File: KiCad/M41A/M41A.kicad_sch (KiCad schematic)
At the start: 22 parts, among them SW1 SW_PWR_ON_OFF

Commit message: Updated scheme
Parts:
- C3: footprint Capacitor_THT:C_Disc_D3.0mm_W2.0mm_P2.50mm -> Capacitor_THT:CP_Radial_D5.0mm_P2.50mm
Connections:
- net at DRV-74HC595.1 (VCC): now also A1.27 (+5V), C1.1, C2.1, D1.1 (K), D2.2 (A), RE1.5 (VCC)
- net at DRV-74HC595.3 (SDD): now also A1.16 (D13)
- net at DRV-74HC595.4 (SCLK): now also A1.14 (D11)
- net at DRV-74HC595.5 (LOAD): now also A1.15 (D12)
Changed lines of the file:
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@@
 			)
 		)
-		(property "Footprint" "Capacitor_THT:C_Disc_D3.0mm_W2.0mm_P2.50mm"
+		(property "Footprint" "Capacitor_THT:CP_Radial_D5.0mm_P2.50mm"
 			(at 74.93 122.8852 0)
 			(effects

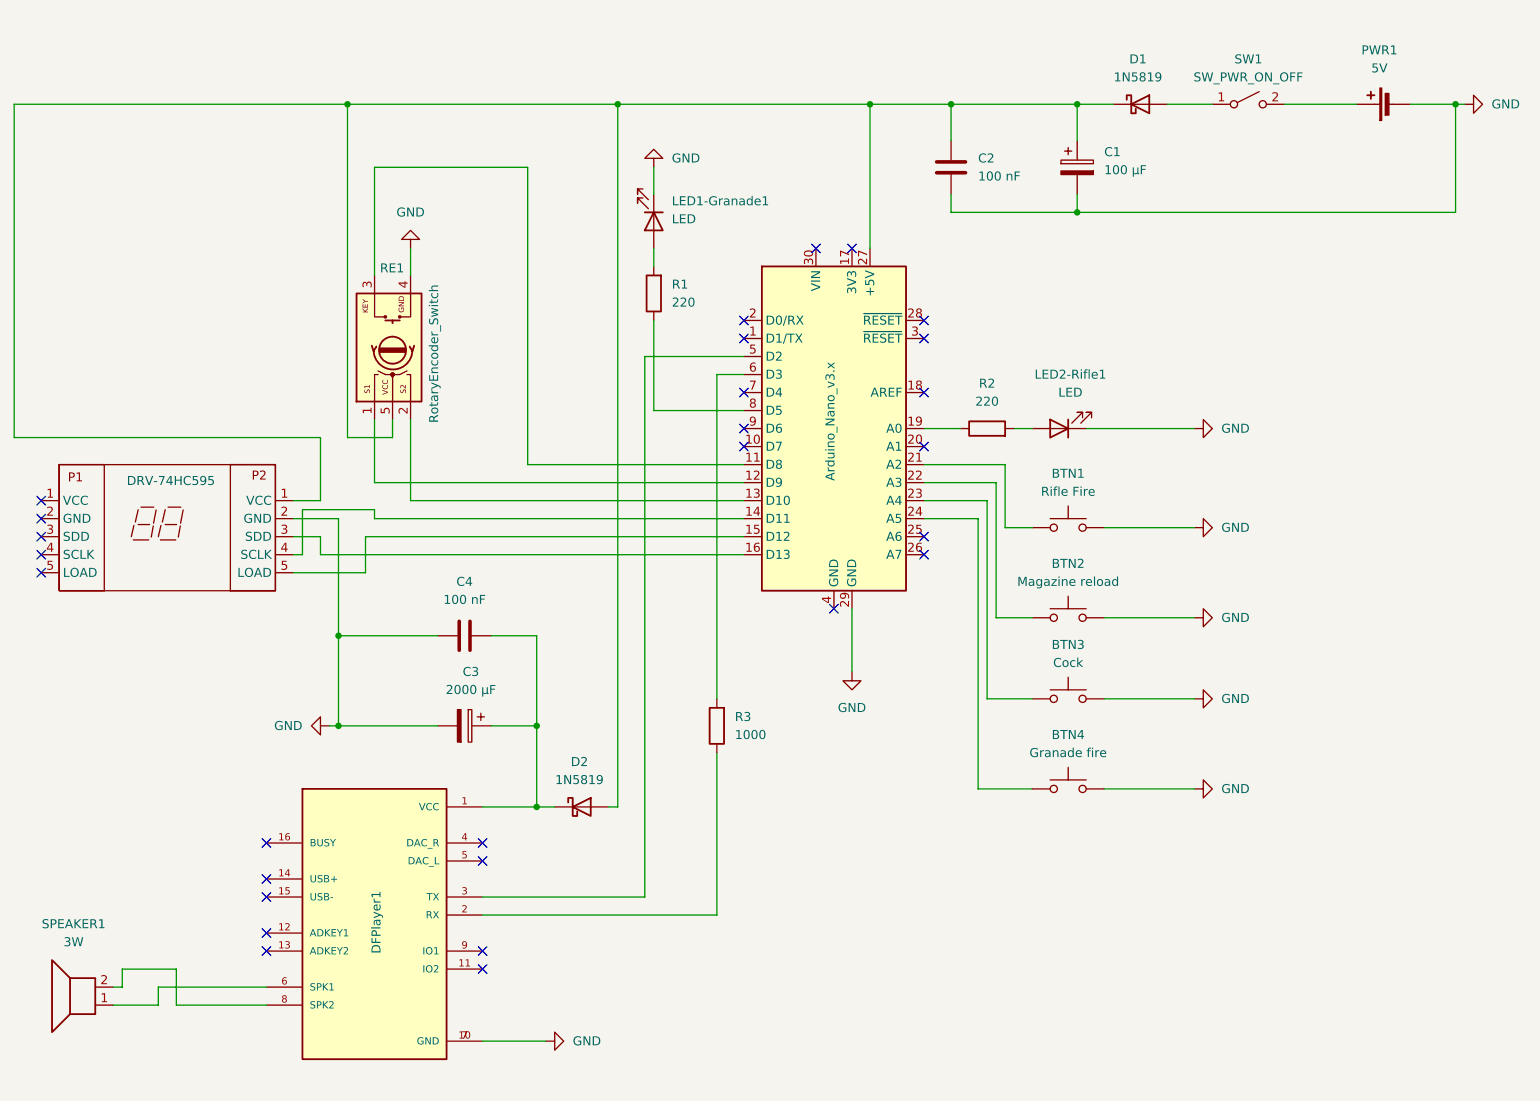
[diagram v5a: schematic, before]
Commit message: Corrected schema wiring between arduino and df player.
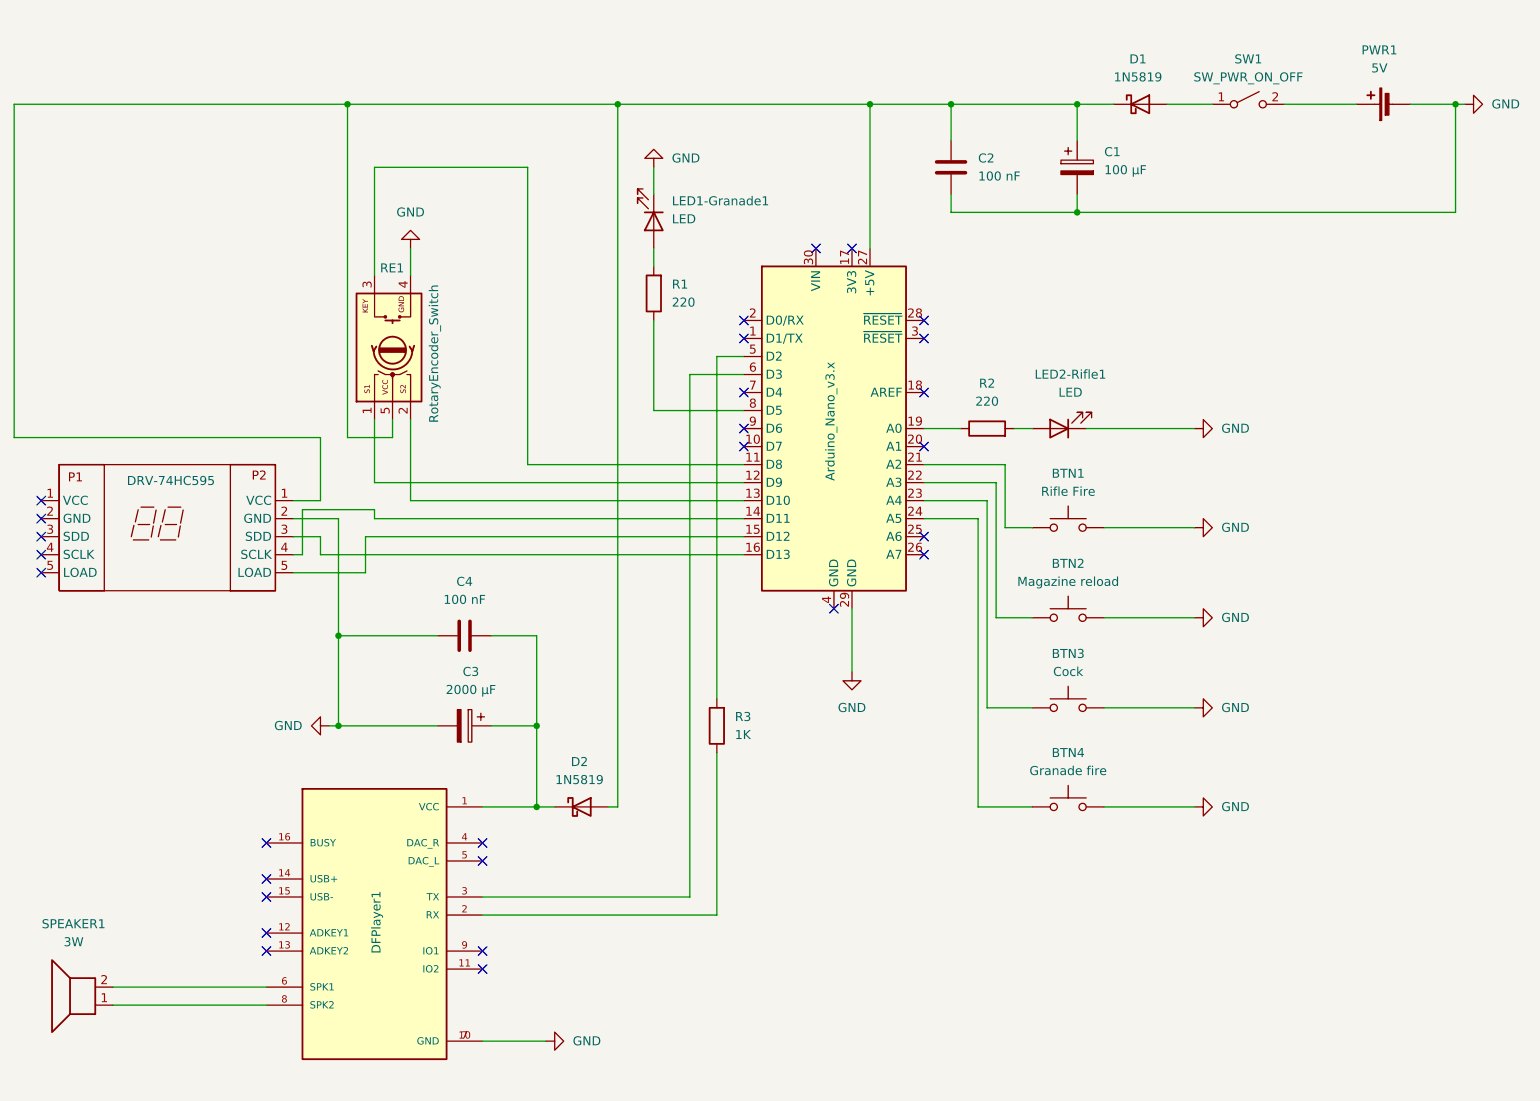
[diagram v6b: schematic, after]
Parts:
- R3: value 1000 -> 1K
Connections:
- net at SPEAKER1.1: now also DFPlayer1.8 (SPK2); no longer DFPlayer1.6 (SPK1)
- net at SPEAKER1.2: now also DFPlayer1.6 (SPK1); no longer DFPlayer1.8 (SPK2)
- net at DRV-74HC595.1 (VCC): now also A1.27 (+5V), C1.1, C2.1, D1.1 (K), D2.2 (A), RE1.5 (VCC)
- net at DRV-74HC595.3 (SDD): now also A1.16 (D13)
- net at DRV-74HC595.4 (SCLK): now also A1.14 (D11)
- net at DRV-74HC595.5 (LOAD): now also A1.15 (D12)
- net at R3.2: now also A1.5 (D2); no longer A1.6 (D3)
- net at DFPlayer1.3 (TX): now also A1.6 (D3); no longer A1.5 (D2)
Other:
- moved on the sheet: BTN3, BTN4
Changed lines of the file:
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@@
 		(date "2024-05-20")
 		(rev "1.1")
-		(comment 1 "https://github.com/ByPS128/Arduino-Aliens-M41A-Riffle")
+		(comment 1 "https://github.com/ByPS128/Arduino-Aliens-M41A-Rifle")
 		(comment 2 "Developer: Petr Škaloud aka ByPS")
 	)
@@
 	(wire
 		(pts
-			(xy 151.13 130.81) (xy 151.13 92.71)
+			(xy 151.13 133.35) (xy 151.13 92.71)
 		)
 		(stroke
@@
 	(wire
 		(pts
-			(xy 152.4 118.11) (xy 158.75 118.11)
+			(xy 152.4 119.38) (xy 158.75 119.38)
 		)
 		(stroke
@@
 	(wire
 		(pts
-			(xy 114.3 72.39) (xy 114.3 118.11)
+			(xy 114.3 69.85) (xy 114.3 118.11)
 		)
 		(stroke
@@
 	(wire
 		(pts
-			(xy 104.14 146.05) (xy 81.28 146.05)
+			(xy 110.49 146.05) (xy 81.28 146.05)
 		)
 		(stroke
@@
 	(wire
 		(pts
-			(xy 66.04 91.44) (xy 66.04 92.71)
+			(xy 110.49 72.39) (xy 110.49 146.05)
 		)
 		(stroke
@@
 	(wire
 		(pts
-			(xy 82.55 109.22) (xy 88.9 109.22)
-		)
-		(stroke
-			(width 0)
-			(type default)
-		)
-	)
-	(wire
-		(pts
-			(xy 143.51 87.63) (xy 153.67 87.63)
+			(xy 66.04 91.44) (xy 66.04 92.71)
 		)
 		(stroke
@@
 	(wire
 		(pts
-			(xy 165.1 34.29) (xy 170.18 34.29)
+			(xy 82.55 109.22) (xy 88.9 109.22)
 		)
 		(stroke
@@
 	(wire
 		(pts
-			(xy 88.9 109.22) (xy 88.9 121.92)
+			(xy 143.51 87.63) (xy 153.67 87.63)
 		)
 		(stroke
@@
 	(wire
 		(pts
-			(xy 35.56 161.29) (xy 29.21 161.29)
+			(xy 165.1 34.29) (xy 170.18 34.29)
 		)
 		(stroke
@@
 	(wire
 		(pts
-			(xy 35.56 158.75) (xy 50.8 158.75)
+			(xy 88.9 109.22) (xy 88.9 121.92)
 		)
 		(stroke
@@
 	(wire
 		(pts
-			(xy 50.8 161.29) (xy 38.1 161.29)
+			(xy 29.21 161.29) (xy 50.8 161.29)
 		)
 		(stroke
@@
 	(wire
 		(pts
-			(xy 35.56 158.75) (xy 35.56 161.29)
-		)
-		(stroke
-			(width 0)
-			(type default)
-		)
-	)
-	(wire
-		(pts
 			(xy 74.93 109.22) (xy 60.96 109.22)
 		)
@@
 	(wire
 		(pts
-			(xy 158.75 130.81) (xy 151.13 130.81)
+			(xy 158.75 133.35) (xy 151.13 133.35)
 		)
 		(stroke
@@
 	(wire
 		(pts
-			(xy 104.14 69.85) (xy 104.14 146.05)
-		)
-		(stroke
-			(width 0)
-			(type default)
-		)
-	)
-	(wire
-		(pts
 			(xy 15.24 34.29) (xy 62.23 34.29)
 		)
@@
 	(wire
 		(pts
-			(xy 114.3 72.39) (xy 118.11 72.39)
-		)
-		(stroke
-			(width 0)
-			(type default)
-		)
-	)
-	(wire
-		(pts
 			(xy 218.44 34.29) (xy 218.44 49.53)
 		)
@@
 	(wire
 		(pts
-			(xy 168.91 130.81) (xy 181.61 130.81)
+			(xy 168.91 133.35) (xy 181.61 133.35)
 		)
 		(stroke
@@
 	(wire
 		(pts
-			(xy 168.91 118.11) (xy 181.61 118.11)
+			(xy 168.91 119.38) (xy 181.61 119.38)
 		)
 		(stroke
@@
 	(wire
 		(pts
-			(xy 166.37 80.01) (xy 181.61 80.01)
+			(xy 110.49 72.39) (xy 118.11 72.39)
 		)
 		(stroke
@@
 	(wire
 		(pts
-			(xy 54.61 100.33) (xy 64.77 100.33)
+			(xy 166.37 80.01) (xy 181.61 80.01)
 		)
 		(stroke
@@
 	(wire
 		(pts
-			(xy 147.32 34.29) (xy 147.32 39.37)
+			(xy 54.61 100.33) (xy 64.77 100.33)
 		)
 		(stroke
@@
 	(wire
 		(pts
-			(xy 88.9 133.35) (xy 91.44 133.35)
+			(xy 147.32 34.29) (xy 147.32 39.37)
 		)
 		(stroke
@@
 	(wire
 		(pts
-			(xy 135.89 34.29) (xy 147.32 34.29)
+			(xy 88.9 133.35) (xy 91.44 133.35)
 		)
 		(stroke
@@
 	(wire
 		(pts
-			(xy 62.23 81.28) (xy 62.23 34.29)
+			(xy 135.89 34.29) (xy 147.32 34.29)
 		)
 		(stroke
@@
 	(wire
 		(pts
-			(xy 147.32 34.29) (xy 165.1 34.29)
+			(xy 62.23 81.28) (xy 62.23 34.29)
 		)
 		(stroke
@@
 	(wire
 		(pts
-			(xy 118.11 69.85) (xy 104.14 69.85)
+			(xy 147.32 34.29) (xy 165.1 34.29)
 		)
 		(stroke
@@
 	(wire
 		(pts
-			(xy 38.1 161.29) (xy 38.1 156.21)
-		)
-		(stroke
-			(width 0)
-			(type default)
-		)
-	)
-	(wire
-		(pts
 			(xy 66.04 87.63) (xy 118.11 87.63)
 		)
@@
 	(wire
 		(pts
-			(xy 30.48 156.21) (xy 30.48 158.75)
-		)
-		(stroke
-			(width 0)
-			(type default)
-		)
-	)
-	(wire
-		(pts
 			(xy 135.89 34.29) (xy 135.89 54.61)
 		)
@@
 	(wire
 		(pts
-			(xy 30.48 158.75) (xy 29.21 158.75)
+			(xy 29.21 158.75) (xy 50.8 158.75)
 		)
 		(stroke
@@
 	(wire
 		(pts
-			(xy 152.4 90.17) (xy 152.4 118.11)
+			(xy 152.4 90.17) (xy 152.4 119.38)
 		)
 		(stroke
@@
 	(wire
 		(pts
-			(xy 38.1 156.21) (xy 30.48 156.21)
+			(xy 153.67 106.68) (xy 158.75 106.68)
 		)
 		(stroke
@@
 	(wire
 		(pts
-			(xy 153.67 106.68) (xy 158.75 106.68)
+			(xy 55.88 91.44) (xy 66.04 91.44)
 		)
 		(stroke
@@
 	(wire
 		(pts
-			(xy 55.88 91.44) (xy 66.04 91.44)
+			(xy 88.9 121.92) (xy 88.9 133.35)
 		)
 		(stroke
@@
 	(wire
 		(pts
-			(xy 88.9 121.92) (xy 88.9 133.35)
+			(xy 212.09 34.29) (xy 218.44 34.29)
 		)
 		(stroke
@@
 	(wire
 		(pts
-			(xy 212.09 34.29) (xy 218.44 34.29)
+			(xy 153.67 87.63) (xy 153.67 106.68)
 		)
 		(stroke
@@
 	(wire
 		(pts
-			(xy 153.67 87.63) (xy 153.67 106.68)
+			(xy 114.3 69.85) (xy 118.11 69.85)
 		)
 		(stroke
@@
 	(symbol
 		(lib_id "Switch:SW_Push")
-		(at 163.83 118.11 0)
+		(at 163.83 119.38 0)
 		(unit 1)
 		(exclude_from_sim no)
@@
 		(fields_autoplaced yes)
 		(property "Reference" "BTN3"
-			(at 163.83 110.49 0)
+			(at 163.83 111.76 0)
 			(effects
 				(font
@@
 		)
 		(property "Value" "Cock"
-			(at 163.83 113.03 0)
+			(at 163.83 114.3 0)
 			(effects
 				(font
@@
 		)
 		(property "Footprint" "ProjectLibrary:Button Leads 2x 2.54"
-			(at 163.83 113.03 0)
+			(at 163.83 114.3 0)
 			(effects
 				(font
@@
 		)
 		(property "Datasheet" "~"
-			(at 163.83 113.03 0)
+			(at 163.83 114.3 0)
 			(effects
 				(font
@@
 		)
 		(property "Description" "Push button switch, generic, two pins"
-			(at 163.83 118.11 0)
+			(at 163.83 119.38 0)
 			(effects
 				(font
@@
 	(symbol
 		(lib_id "power:GND")
-		(at 181.61 130.81 90)
+		(at 181.61 133.35 90)
 		(unit 1)
 		(exclude_from_sim no)
@@
 		(fields_autoplaced yes)
 		(property "Reference" "#PWR09"
-			(at 187.96 130.81 0)
+			(at 187.96 133.35 0)
 			(effects
 				(font
@@
 		)
 		(property "Value" "GND"
-			(at 185.42 130.8099 90)
+			(at 185.42 133.3499 90)
 			(effects
 				(font
@@
 		)
 		(property "Footprint" ""
-			(at 181.61 130.81 0)
+			(at 181.61 133.35 0)
 			(effects
 				(font
@@
 		)
 		(property "Datasheet" ""
-			(at 181.61 130.81 0)
+			(at 181.61 133.35 0)
 			(effects
 				(font
@@
 		)
 		(property "Description" "Power symbol creates a global label with name \"GND\" , ground"
-			(at 181.61 130.81 0)
+			(at 181.61 133.35 0)
 			(effects
 				(font
@@
 			)
 		)
-		(property "Value" "1000"
+		(property "Value" "1K"
 			(at 116.84 123.1899 0)
 			(effects
@@
 	(symbol
 		(lib_id "power:GND")
-		(at 181.61 118.11 90)
+		(at 181.61 119.38 90)
 		(unit 1)
 		(exclude_from_sim no)
@@
 		(fields_autoplaced yes)
 		(property "Reference" "#PWR08"
-			(at 187.96 118.11 0)
+			(at 187.96 119.38 0)
 			(effects
 				(font
@@
 		)
 		(property "Value" "GND"
-			(at 185.42 118.1099 90)
+			(at 185.42 119.3799 90)
 			(effects
 				(font
@@
 		)
 		(property "Footprint" ""
-			(at 181.61 118.11 0)
+			(at 181.61 119.38 0)
 			(effects
 				(font
@@
 		)
 		(property "Datasheet" ""
-			(at 181.61 118.11 0)
+			(at 181.61 119.38 0)
 			(effects
 				(font
@@
 		)
 		(property "Description" "Power symbol creates a global label with name \"GND\" , ground"
-			(at 181.61 118.11 0)
+			(at 181.61 119.38 0)
 			(effects
 				(font
@@
 	(symbol
 		(lib_id "Switch:SW_Push")
-		(at 163.83 130.81 0)
+		(at 163.83 133.35 0)
 		(unit 1)
 		(exclude_from_sim no)
@@
 		(fields_autoplaced yes)
 		(property "Reference" "BTN4"
-			(at 163.83 123.19 0)
+			(at 163.83 125.73 0)
 			(effects
 				(font
@@
 		)
 		(property "Value" "Granade fire"
-			(at 163.83 125.73 0)
+			(at 163.83 128.27 0)
 			(effects
 				(font
@@
 		)
 		(property "Footprint" "ProjectLibrary:Button Leads 2x 2.54"
-			(at 163.83 125.73 0)
+			(at 163.83 128.27 0)
 			(effects
 				(font
@@
 		)
 		(property "Datasheet" "~"
-			(at 163.83 125.73 0)
+			(at 163.83 128.27 0)
 			(effects
 				(font
@@
 		)
 		(property "Description" "Push button switch, generic, two pins"
-			(at 163.83 130.81 0)
+			(at 163.83 133.35 0)
 			(effects
 				(font

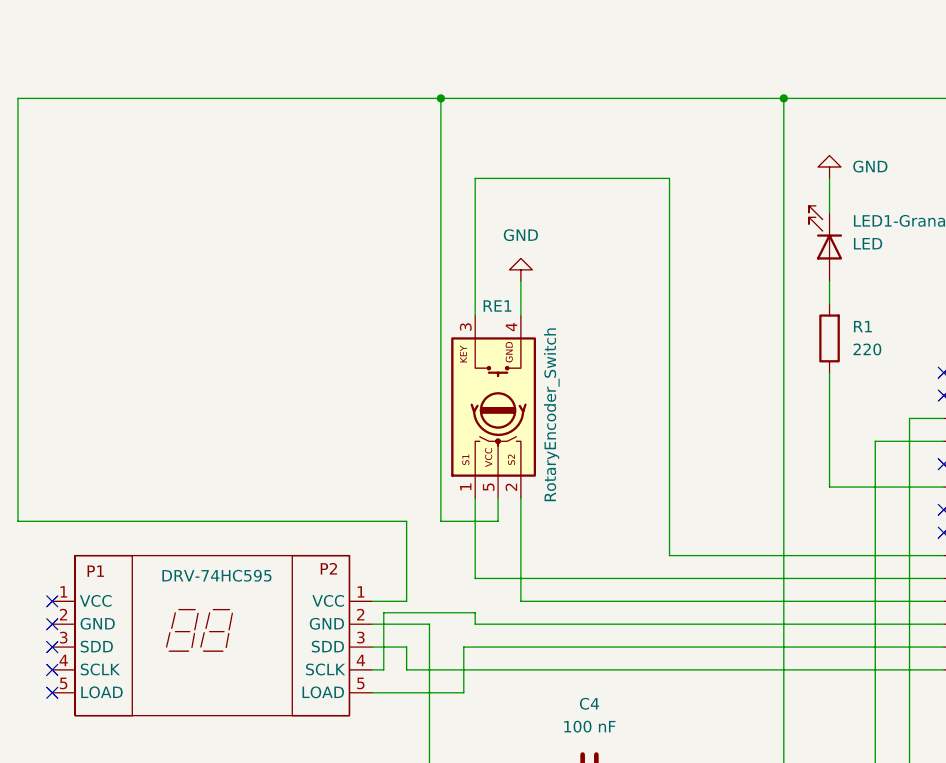
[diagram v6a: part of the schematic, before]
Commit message: Colored schematic wiring for better orientation.
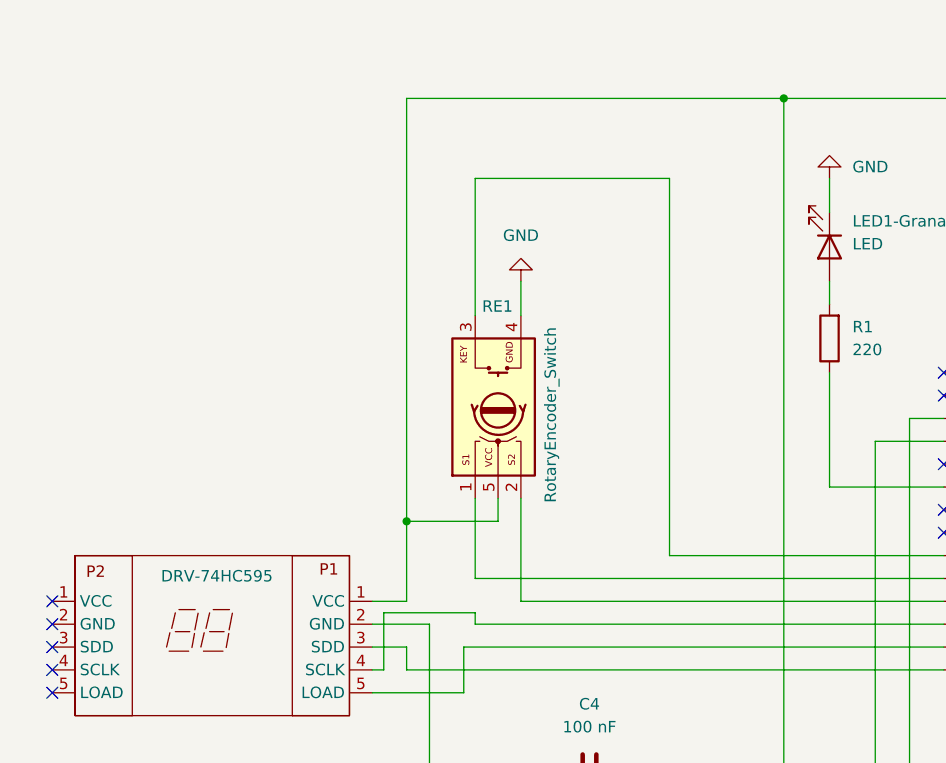
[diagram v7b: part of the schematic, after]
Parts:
- DRV-74HC595: footprint ProjectLibrary:Segment Display Leads 5x 2.54 -> Connector_PinHeader_1.00mm:PinHeader_1x05_P1.00mm_Vertical
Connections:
- net at DRV-74HC595.1 (VCC): now also A1.27 (+5V), C1.1, C2.1, D1.1 (K), D2.2 (A), RE1.5 (VCC)
- net at DRV-74HC595.3 (SDD): now also A1.16 (D13)
- net at DRV-74HC595.4 (SCLK): now also A1.14 (D11)
- net at DRV-74HC595.5 (LOAD): now also A1.15 (D12)
